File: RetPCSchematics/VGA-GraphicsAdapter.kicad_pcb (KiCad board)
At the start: 2 copper layers, 136.7 x 101.3 mm, 42 parts, among them J1 Bus_ISA_8bit, J2 74320-9004, J3 Conn_01x02_Male, U1 74AUC2G125, U10 ATmega644P-20PU, U11 IS61LV5128AL-10TLI, U12 74LS245, U13 SN74LVC245AN, U15 74LVC2G240, U16 74LVC2G240, U17 74LVC1G18, U18 74LVC1G18, U19 74LVC1G18, U2 74LVC2G240, U20 74LVC1G18, U21 ATF22V10D, U22 74LS245A, U23 74LVC1G373, U24 74LVC1G373, U25 74LVC1G373, U26 74LVC1G373, U27 74LVC1G373, U28 74LVC1G373, U29 74LVC1G373, U3 ATF22V10D, U30 74LVC1G373, U31 74LVC1G373, U32 74LVC1G373, U33 74LVC1G373, U34 74LVC1G373, U36 TFP410, U37 ATF750C, U4 ATF22V10D, U5 74LS245, U6 ATF22V10D, U7 74LS245A, U8 74LS245, U9 74LS245A, X1 DGOF5S3

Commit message: routed data lines on video plexing unit
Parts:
- moved U17 25.4 mm to (188.8, 71.2), turned to 0 degrees
- moved U30 24.0 mm to (189.8, 91.5), turned to 0 degrees
- moved U28 22.3 mm to (188.8, 85.9), turned to 0 degrees
- moved U18 22.0 mm to (188.8, 74.9), turned to 0 degrees
- moved U19 21.9 mm to (188.8, 78.5), turned to 0 degrees
- moved U31 21.8 mm to (195.4, 69.4), turned to 0 degrees
- moved U20 21.2 mm to (188.8, 82.2), turned to 0 degrees
- moved U29 18.8 mm to (195.3, 89.1), turned to 0 degrees
- moved U23 17.8 mm to (195.4, 65.8), turned to 0 degrees
- moved U33 14.8 mm to (202.9, 77.4), turned to 0 degrees
- moved U26 14.6 mm to (195.4, 80.8), turned to 0 degrees
- moved U25 12.8 mm to (195.4, 76.7), turned to 0 degrees
- moved U24 11.4 mm to (195.4, 73.1), turned to 0 degrees
- moved U27 11.2 mm to (202.9, 81.1), turned to 0 degrees
- moved U34 11.0 mm to (195.5, 84.9), turned to 0 degrees
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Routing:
- net GClock: track 15.5 -> 127.2 mm, vias 1 -> 15
- net Net-(U16-Pad3): track 0.00 -> 100.2 mm, vias 0 -> 12
- net /VA17: track 30.0 -> 102.7 mm, vias 2 -> 8
- net Net-(U34-Pad4): track 1.00 -> 61.6 mm, vias 0 -> 5
- net Net-(U30-Pad4): track 2.00 -> 60.4 mm, vias 0 -> 6
- net Net-(U23-Pad4): track 2.80 -> 59.2 mm, vias 0 -> 5
- net +3V3: track 208.4 -> 262.3 mm, vias 20 -> 36
- net Net-(U28-Pad4): track 1.14 -> 51.9 mm, vias 0 -> 7
- net Net-(U31-Pad4): track 1.33 -> 51.4 mm, vias 0 -> 3
- net Net-(U29-Pad4): track 5.26 -> 52.6 mm, vias 0 -> 4
- net GEnd(inv): track 0.00 -> 46.3 mm, vias 0 -> 3
- net Net-(U24-Pad4): track 2.00 -> 44.8 mm, vias 0 -> 5
- net Net-(U25-Pad4): track 0.00 -> 42.2 mm, vias 0 -> 4
- net Net-(U26-Pad4): track 0.00 -> 37.9 mm, vias 0 -> 4
- net Net-(U32-Pad4): track 2.56 -> 39.1 mm, vias 0 -> 3
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- added copper zone on F.Cu, net GND
- removed copper zone on F.Cu, net GClock

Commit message: Rev 4.0 done
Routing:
- net GND: track 274.4 -> 445.3 mm, vias 11 -> 21
- net GClock: track 127.2 -> 217.8 mm, vias 15 -> 26
- net +3V3: track 262.3 -> 330.0 mm, vias 36 -> 46
- net Net-(J2-PadSH): track 0.00 -> 34.8 mm
- net /VA4: track 117.4 -> 85.5 mm, vias 5 -> 4
- net LoadEnable: track 218.5 -> 193.0 mm, vias 12 -> 10
- net /D1: track 93.0 -> 99.0 mm, vias 5 -> 6
- net /VA13: track 65.1 -> 60.9 mm
- net /VA3: track 91.2 -> 87.5 mm, vias 6 -> 5
- net /VA2: track 90.5 -> 87.6 mm, vias 6 -> 5
- net /VA1: track 90.1 -> 87.9 mm, vias 5 -> 4
- net Net-(U28-Pad4): track 51.9 -> 52.9 mm
- net /VA14: track 60.3 -> 60.9 mm

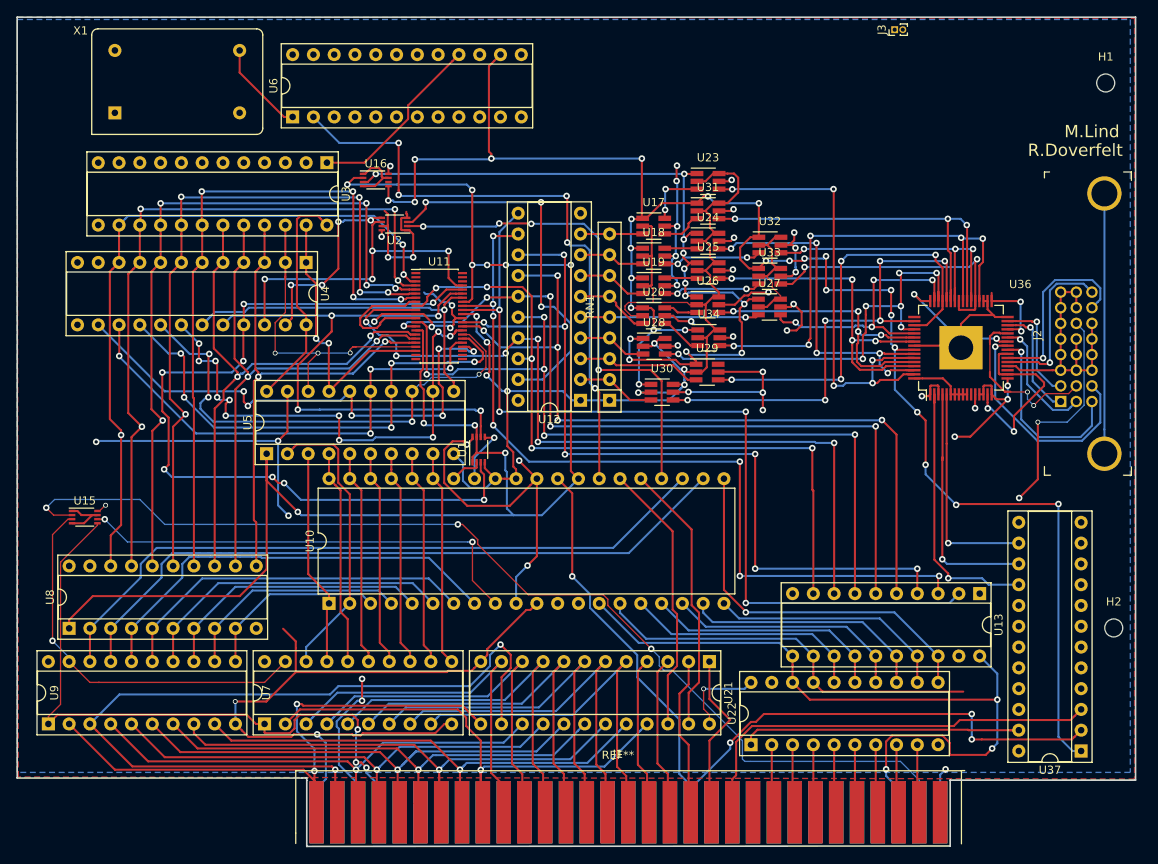
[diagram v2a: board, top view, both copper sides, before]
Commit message: Changed power pin head, added silklayer stuff
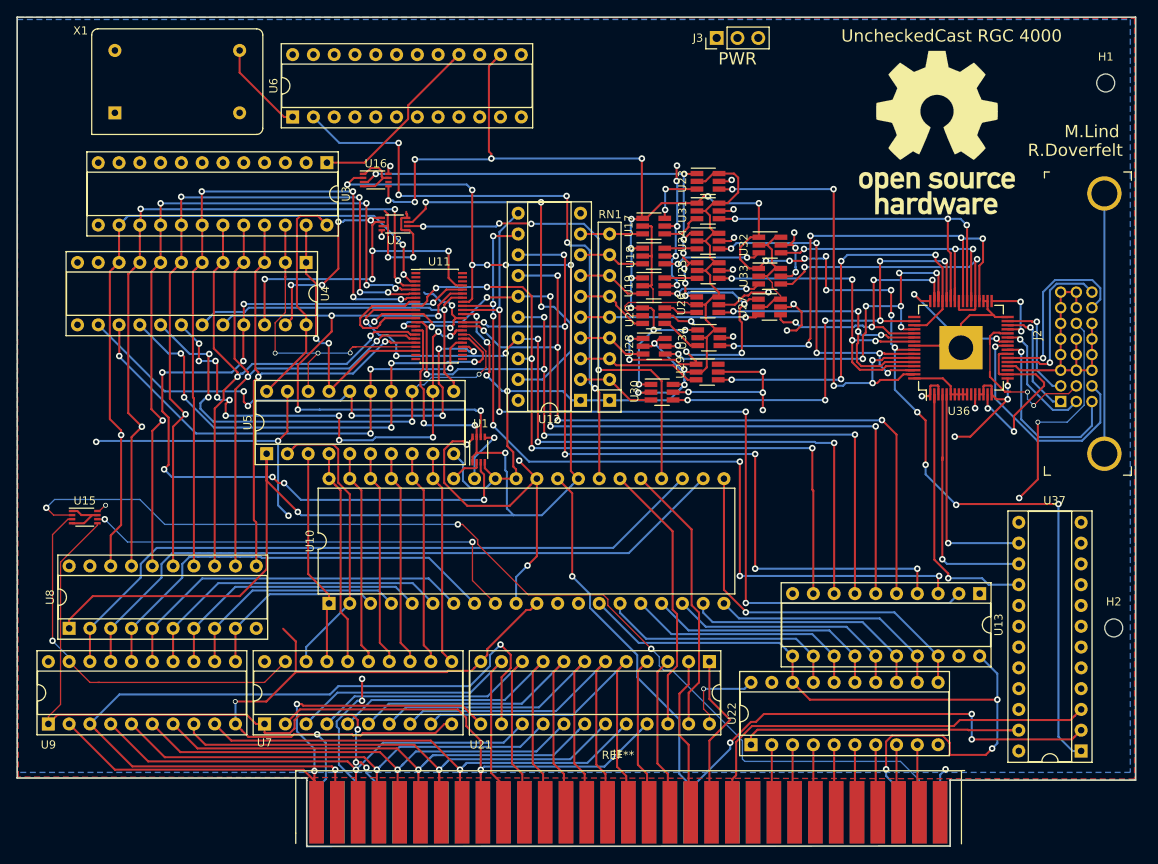
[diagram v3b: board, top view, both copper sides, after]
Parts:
- added REF**: OSHW-Logo_19x20mm_SilkScreen, Symbol:OSHW-Logo_19x20mm_SilkScreen, F.Cu at (223.4, 59.8)
- J3: value Conn_01x02_Male -> PinHeader_1x03_P2.54mm_Vertical; footprint Connector_PinHeader_1.00mm:PinHeader_1x02_P1.00mm_Vertical -> Connector_PinHeader_2.54mm:PinHeader_1x03_P2.54mm_Vertical
- moved J3 21.8 mm to (196.5, 48.3)
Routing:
- net Net-(U10-Pad15): track 49.0 -> 30.2 mm
- net /A8: track 63.0 -> 58.5 mm
- net ALEN: track 80.8 -> 83.3 mm
- net /A4: track 62.6 -> 60.5 mm
- net /A5: track 60.8 -> 62.5 mm
- net +3V3: track 330.0 -> 329.0 mm
- net /A6: track 64.5 -> 65.1 mm
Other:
- board text added: "PWR"
- board text added: "UncheckedCast RGC 4000"

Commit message: Finalized card, ps ordered it too ds
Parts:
- added C1: C, Capacitor_THT:CP_Radial_D4.0mm_P1.50mm, F.Cu at (182.9, 66.8)
- added C10: C, Capacitor_THT:CP_Radial_D4.0mm_P1.50mm, F.Cu at (142.4, 108.9)
- added C2: C, Capacitor_THT:CP_Radial_D4.0mm_P1.50mm, F.Cu at (163.9, 72.8)
- added C3: C, Capacitor_THT:CP_Radial_D4.0mm_P1.50mm, F.Cu at (121.0, 88.1)
- added C4: C, Capacitor_THT:CP_Radial_D4.0mm_P1.50mm, F.Cu at (231.3, 76.1)
- added C5: C, Capacitor_THT:CP_Radial_D4.0mm_P1.50mm, F.Cu at (227.6, 128.0)
- added C6: C, Capacitor_THT:CP_Radial_D4.0mm_P1.50mm, F.Cu at (233.0, 95.1)
- added C7: C, Capacitor_THT:CP_Radial_D4.0mm_P1.50mm, F.Cu at (150.6, 84.6)
- J3: value PinHeader_1x03_P2.54mm_Vertical -> Conn_01x03_Male
- moved REF** 0.74 mm to (222.6, 59.8)
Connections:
- net Net-(J2-Pad1) renamed TX2-
- net Net-(J2-Pad10) renamed TX1+
- net Net-(J2-Pad17) renamed TX0-
- net Net-(J2-Pad18) renamed TX0+
- net Net-(J2-Pad2) renamed TX2+
- net Net-(J2-Pad23) renamed TXC+
- net Net-(J2-Pad24) renamed TXC-
- net Net-(J2-Pad9) renamed TX1-
- J1 pad 10: Net-(J1-Pad10) -> GND
- J1 pad 11: Net-(J1-Pad11) -> MemW
- J1 pad 12: Net-(J1-Pad12) -> (no net)
- J1 pad 14: Net-(J1-Pad14) -> IOR
- J1 pad 15: Net-(J1-Pad15) -> (no net)
- J1 pad 16: Net-(J1-Pad16) -> (no net)
- J1 pad 17: Net-(J1-Pad17) -> (no net)
- J1 pad 18: Net-(J1-Pad18) -> (no net)
- J1 pad 19: Net-(J1-Pad19) -> (no net)
- J1 pad 20: Net-(J1-Pad20) -> (no net)
- J1 pad 21: Net-(J1-Pad21) -> (no net)
- J1 pad 22: Net-(J1-Pad22) -> (no net)
- J1 pad 23: Net-(J1-Pad23) -> (no net)
- J1 pad 24: Net-(J1-Pad24) -> (no net)
- J1 pad 25: Net-(J1-Pad25) -> (no net)
- J1 pad 26: Net-(J1-Pad26) -> (no net)
- J1 pad 27: Net-(J1-Pad27) -> (no net)
- J1 pad 29: +3V3 -> (no net)
- J1 pad 3: +3V3 -> +FEMV
- J1 pad 30: Net-(J1-Pad30) -> (no net)
- J1 pad 32: Net-(J1-Pad32) -> (no net)
- J1 pad 4: Net-(J1-Pad4) -> (no net)
- J1 pad 41: Net-(J1-Pad41) -> (no net)
- J1 pad 5: Net-(J1-Pad5) -> (no net)
- J1 pad 6: Net-(J1-Pad6) -> (no net)
- J1 pad 7: Net-(J1-Pad7) -> (no net)
- J1 pad 8: Net-(J1-Pad8) -> (no net)
- J1 pad 9: Net-(J1-Pad9) -> (no net)
- J2 pad 14: +3V3 -> +FEMV
- U10 pad 12: Net-(U10-Pad12) -> (no net)
- U10 pad 13: Net-(U10-Pad13) -> (no net)
- U10 pad 26: REG -> Dir
- U10 pad 29: IOW -> busr
- U11 pad 1: Net-(U11-Pad1) -> (no net)
- U11 pad 2: Net-(U11-Pad2) -> (no net)
- U11 pad 21: Net-(U11-Pad21) -> (no net)
- U11 pad 22: Net-(U11-Pad22) -> (no net)
- U11 pad 23: Net-(U11-Pad23) -> (no net)
- U11 pad 24: Net-(U11-Pad24) -> (no net)
- U11 pad 25: Net-(U11-Pad25) -> (no net)
- U11 pad 37: LoadEnable -> (inv)LE
- U11 pad 42: Net-(U11-Pad42) -> (no net)
- U11 pad 43: Net-(U11-Pad43) -> (no net)
- U11 pad 44: Net-(U11-Pad44) -> (no net)
- U13 pad 1: Net-(U13-Pad1) -> GND
- U13 pad 19: Net-(U13-Pad19) -> LoadEnable
- U21 pad 22: REG -> (no net)
- U22 pad 1: DR -> Dir
- U22 pad 19: GND -> Sel
- U29 pad 6: Net-(U29-Pad6) -> GND
- U3 pad 10: Net-(U3-Pad10) -> (no net)
- U3 pad 11: Net-(U3-Pad11) -> (no net)
- U3 pad 13: Net-(U3-Pad13) -> (no net)
- U3 pad 2: Net-(U3-Pad2) -> (no net)
- U3 pad 3: Net-(U3-Pad3) -> (no net)
- U3 pad 4: Net-(U3-Pad4) -> (no net)
- U3 pad 5: Net-(U3-Pad5) -> (no net)
- U3 pad 6: Net-(U3-Pad6) -> (no net)
- U3 pad 7: Net-(U3-Pad7) -> (no net)
- U3 pad 8: Net-(U3-Pad8) -> (no net)
- U3 pad 9: Net-(U3-Pad9) -> (no net)
- U36 pad 11: Net-(U36-Pad11) -> (no net)
- U36 pad 19: Net-(U36-Pad19) -> (no net)
- U36 pad 49: Net-(U36-Pad49) -> (no net)
- U37 pad 10: Net-(U37-Pad10) -> (no net)
- U37 pad 11: Net-(U37-Pad11) -> (no net)
- U37 pad 13: Net-(U37-Pad13) -> (no net)
- U37 pad 17: Net-(U37-Pad17) -> busr
- U37 pad 18: Net-(U37-Pad18) -> (no net)
- U37 pad 19: Net-(U37-Pad19) -> (no net)
- U37 pad 20: Net-(U37-Pad20) -> (no net)
- U37 pad 21: Net-(U37-Pad21) -> (no net)
- U37 pad 22: Net-(U37-Pad22) -> (no net)
- U37 pad 23: DR -> (no net)
- U37 pad 4: Net-(U37-Pad4) -> IOR
- U37 pad 5: Net-(U37-Pad5) -> MemW
- U37 pad 6: Net-(U37-Pad6) -> (no net)
- U37 pad 7: Net-(U37-Pad7) -> (no net)
- U37 pad 8: Net-(U37-Pad8) -> (no net)
- U37 pad 9: Net-(U37-Pad9) -> (no net)
- U4 pad 11: Net-(U4-Pad11) -> (no net)
- U4 pad 13: Net-(U4-Pad13) -> (no net)
- U5 pad 1: LoadEnable -> (inv)LE
- U6 pad 10: Net-(U6-Pad10) -> (no net)
- U6 pad 11: Net-(U6-Pad11) -> (no net)
- U6 pad 13: Net-(U6-Pad13) -> (no net)
- U6 pad 15: Net-(U6-Pad15) -> (no net)
- U6 pad 17: Net-(U6-Pad17) -> (no net)
- U6 pad 18: Net-(U6-Pad18) -> (no net)
- U6 pad 19: Net-(U6-Pad19) -> (no net)
- U6 pad 20: Net-(U6-Pad20) -> (no net)
- U6 pad 21: Net-(U6-Pad21) -> (no net)
- U6 pad 22: Net-(U6-Pad22) -> (no net)
- U6 pad 23: Net-(U6-Pad23) -> (no net)
- U6 pad 3: Net-(U6-Pad3) -> (no net)
- U6 pad 4: Net-(U6-Pad4) -> (no net)
- U6 pad 5: Net-(U6-Pad5) -> (no net)
- U6 pad 6: Net-(U6-Pad6) -> (no net)
- U6 pad 7: Net-(U6-Pad7) -> (no net)
- U6 pad 8: Net-(U6-Pad8) -> (no net)
- U6 pad 9: Net-(U6-Pad9) -> (no net)
- U8 pad 1: LoadEnable -> (inv)LE
- X1 pad 1: Net-(X1-Pad1) -> (no net)
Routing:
- net (inv)LE: track 0.00 -> 153.1 mm, vias 0 -> 5
- net +3V3: track 329.0 -> 237.2 mm, vias 46 -> 41
- net +FEMV: track 0.00 -> 80.3 mm, vias 0 -> 5
- net IOR: track 0.00 -> 77.0 mm, vias 0 -> 3
- net busr: track 0.00 -> 71.1 mm, vias 0 -> 3
- net MemW: track 0.00 -> 57.0 mm, vias 0 -> 3
- net Dir: track 0.00 -> 42.2 mm, vias 0 -> 3
- net GND: track 445.3 -> 486.7 mm, vias 21 -> 24
- net DR: track 35.3 -> 0.00 mm
- net REG: track 33.3 -> 0.00 mm
- net ALEN(inv): track 48.2 -> 69.6 mm
- net GEnd: track 23.7 -> 43.6 mm, vias 4 -> 6
- net TXC-: track 20.1 -> 32.6 mm, vias 1 -> 0
- net IOW: track 105.2 -> 94.2 mm
- net TX0+: track 28.7 -> 18.3 mm, vias 1 -> 0
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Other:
- net class Default: clearance 0.2 -> 0.15
- net class smol: clearance 0.2 -> 0.15
- rule trace_clearance: 0.2 -> 0.15
